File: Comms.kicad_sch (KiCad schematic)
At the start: 29 parts, among them J2 RJ45_Wuerth_7499010121A, Y1 25M

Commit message: assigned footprints
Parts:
- C1, C10, C11, C12, C13, C2, C3, C4, C5, C6, C7, C8, C9: footprint (none) -> Capacitor_SMD:C_0603_1608Metric
- D1, D2, D3, D4: footprint (none) -> LED_SMD:LED_0603_1608Metric
- R1, R2, R3, R4, R5, R6, R7, R9: footprint (none) -> Resistor_SMD:R_0603_1608Metric
- U1: footprint (none) -> Package_QFP:LQFP-64_10x10mm_P0.5mm
- Y1: footprint (none) -> Crystal:Crystal_SMD_7050-4Pin_7.0x5.0mm
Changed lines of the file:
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@@
 			)
 		)
-		(property "Footprint" ""
+		(property "Footprint" "Capacitor_SMD:C_0603_1608Metric"
 			(at 154.94 160.02 0)
 			(effects
@@
 			)
 		)
-		(property "Footprint" ""
+		(property "Footprint" "Capacitor_SMD:C_0603_1608Metric"
 			(at 109.22 171.45 0)
 			(effects
@@
 			)
 		)
-		(property "Footprint" ""
+		(property "Footprint" "LED_SMD:LED_0603_1608Metric"
 			(at 245.11 50.8 0)
 			(effects
@@
 			)
 		)
-		(property "Footprint" ""
+		(property "Footprint" "Capacitor_SMD:C_0603_1608Metric"
 			(at 243.84 99.06 0)
 			(effects
@@
 			)
 		)
-		(property "Footprint" ""
+		(property "Footprint" "Capacitor_SMD:C_0603_1608Metric"
 			(at 257.81 69.85 0)
 			(effects
@@
 			)
 		)
-		(property "Footprint" ""
+		(property "Footprint" "Capacitor_SMD:C_0603_1608Metric"
 			(at 154.94 152.4 0)
 			(effects
@@
 			)
 		)
-		(property "Footprint" ""
+		(property "Footprint" "Resistor_SMD:R_0603_1608Metric"
 			(at 259.08 30.48 0)
 			(effects
@@
 			)
 		)
-		(property "Footprint" ""
+		(property "Footprint" "Resistor_SMD:R_0603_1608Metric"
 			(at 93.98 149.86 0)
 			(effects
@@
 			)
 		)
-		(property "Footprint" ""
+		(property "Footprint" "LED_SMD:LED_0603_1608Metric"
 			(at 245.11 30.48 0)
 			(effects
@@
 			)
 		)
-		(property "Footprint" ""
+		(property "Footprint" "Package_QFP:LQFP-64_10x10mm_P0.5mm"
 			(at 74.93 60.96 0)
 			(effects
@@
 			)
 		)
-		(property "Footprint" ""
+		(property "Footprint" "Resistor_SMD:R_0603_1608Metric"
 			(at 259.08 50.8 0)
 			(effects
@@
 			)
 		)
-		(property "Footprint" ""
+		(property "Footprint" "Crystal:Crystal_SMD_7050-4Pin_7.0x5.0mm"
 			(at 246.38 76.2 0)
 			(effects
@@
 			)
 		)
-		(property "Footprint" ""
+		(property "Footprint" "Resistor_SMD:R_0603_1608Metric"
 			(at 184.15 34.29 0)
 			(effects
@@
 			)
 		)
-		(property "Footprint" ""
+		(property "Footprint" "Resistor_SMD:R_0603_1608Metric"
 			(at 95.25 160.02 0)
 			(effects
@@
 			)
 		)
-		(property "Footprint" ""
+		(property "Footprint" "Capacitor_SMD:C_0603_1608Metric"
 			(at 233.68 99.06 0)
 			(effects
@@
 			)
 		)
-		(property "Footprint" ""
+		(property "Footprint" "Resistor_SMD:R_0603_1608Metric"
 			(at 259.08 45.72 0)
 			(effects
@@
 			)
 		)
-		(property "Footprint" ""
+		(property "Footprint" "Capacitor_SMD:C_0603_1608Metric"
 			(at 223.52 99.06 0)
 			(effects
@@
 			)
 		)
-		(property "Footprint" ""
+		(property "Footprint" "Capacitor_SMD:C_0603_1608Metric"
 			(at 166.37 67.31 0)
 			(effects
@@
 			)
 		)
-		(property "Footprint" ""
+		(property "Footprint" "LED_SMD:LED_0603_1608Metric"
 			(at 245.11 25.4 0)
 			(effects
@@
 			)
 		)
-		(property "Footprint" ""
+		(property "Footprint" "Resistor_SMD:R_0603_1608Metric"
 			(at 182.88 58.42 0)
 			(effects
@@
 			)
 		)
-		(property "Footprint" ""
+		(property "Footprint" "Capacitor_SMD:C_0603_1608Metric"
 			(at 257.81 82.55 0)
 			(effects
@@
 			)
 		)
-		(property "Footprint" ""
+		(property "Footprint" "Capacitor_SMD:C_0603_1608Metric"
 			(at 265.43 99.06 0)
 			(effects
@@
 			)
 		)
-		(property "Footprint" ""
+		(property "Footprint" "Capacitor_SMD:C_0603_1608Metric"
 			(at 255.27 99.06 0)
 			(effects
@@
 			)
 		)
-		(property "Footprint" ""
+		(property "Footprint" "Capacitor_SMD:C_0603_1608Metric"
 			(at 123.19 39.37 0)
 			(effects
@@
 			)
 		)
-		(property "Footprint" ""
+		(property "Footprint" "Capacitor_SMD:C_0603_1608Metric"
 			(at 166.37 90.17 0)
 			(effects
@@
 			)
 		)
-		(property "Footprint" ""
+		(property "Footprint" "Resistor_SMD:R_0603_1608Metric"
 			(at 259.08 25.4 0)
 			(effects
@@
 			)
 		)
-		(property "Footprint" ""
+		(property "Footprint" "LED_SMD:LED_0603_1608Metric"
 			(at 245.11 45.72 0)
 			(effects

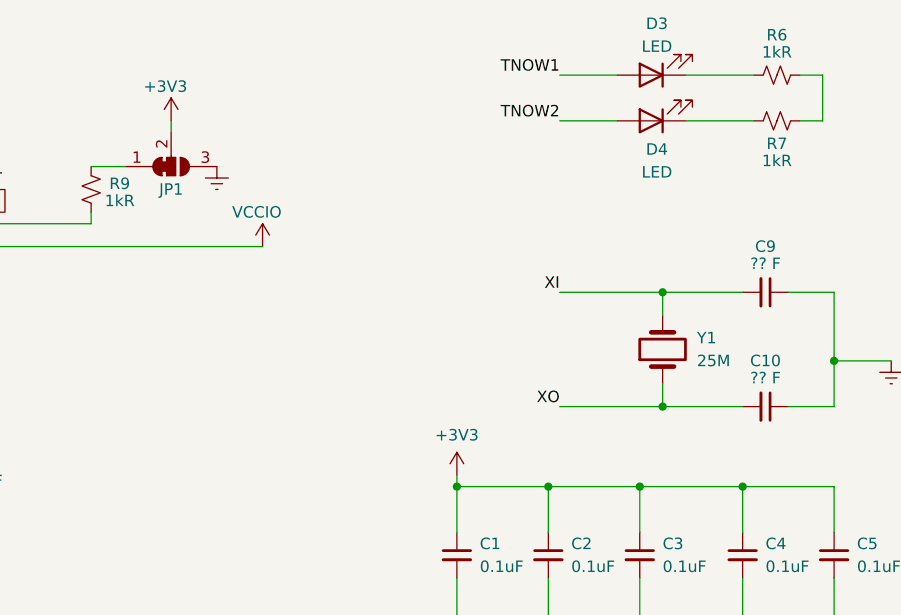
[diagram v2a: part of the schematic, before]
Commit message: routed besides mcu connections and pwoer
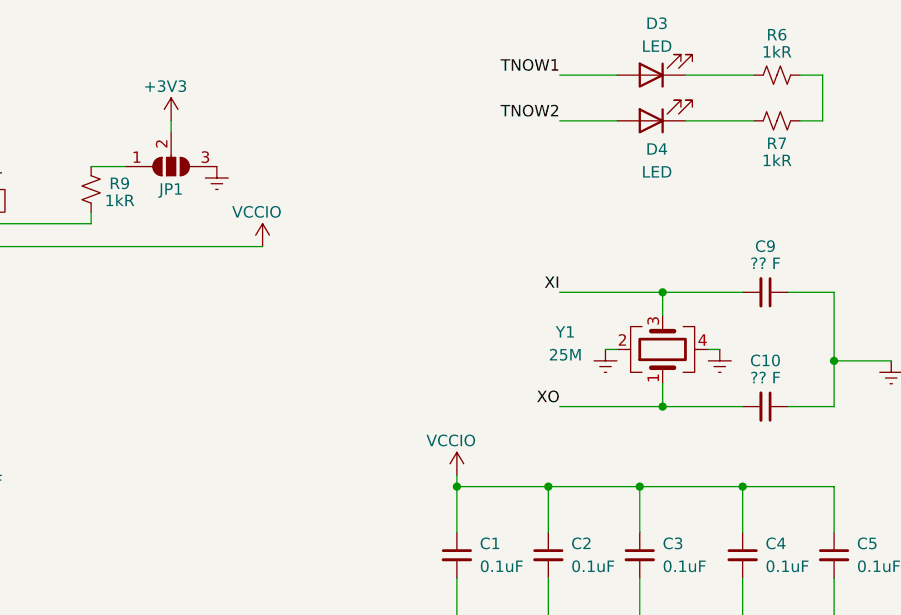
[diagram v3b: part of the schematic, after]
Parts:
- removed JP1: SolderJumper_3_Bridged12, symbol Jumper:SolderJumper_3_Bridged12
- removed Y1: 25M, Crystal:Crystal_SMD_7050-4Pin_7.0x5.0mm, symbol Device:Crystal
- added JP1: SolderJumper_3_Open, Jumper:SolderJumper-3_P1.3mm_Open_RoundedPad1.0x1.5mm_NumberLabels, symbol Jumper:SolderJumper_3_Open
- added Y1: 25M, Crystal:Crystal_SMD_7050-4Pin_7.0x5.0mm, symbol Device:Crystal_GND24
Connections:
- net +3V3: now also JP1.2 (C); no longer C1.1, C2.1, C3.1, C4.1, C5.1
- net GND: now also JP1.3 (B), Y1.2, Y1.4
- net VCCIO: now also C1.1, C2.1, C3.1, C4.1, C5.1
- net XI: now also Y1.3
- net XO: now also Y1.1
- net at R9.1: now also JP1.1 (A)

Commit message: done with my subsystem
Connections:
- net GND: now also R6.2, R7.2
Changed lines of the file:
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@@
 	)
 	(junction
+		(at 264.16 50.8)
+		(diameter 0)
+		(color 0 0 0 0)
+	)
+	(junction
 		(at 168.91 92.71)
 		(diameter 0)
@@
 	(wire
 		(pts
+			(xy 266.7 50.8) (xy 264.16 50.8)
+		)
+		(stroke
+			(width 0)
+			(type default)
+		)
+	)
+	(wire
+		(pts
 			(xy 128.27 27.94) (xy 128.27 45.72)
 		)
@@
 	(wire
 		(pts
+			(xy 266.7 52.07) (xy 266.7 50.8)
+		)
+		(stroke
+			(width 0)
+			(type default)
+		)
+	)
+	(wire
+		(pts
 			(xy 80.01 82.55) (xy 99.06 82.55)
 		)
@@
 					(unit 1)
 				)
+			)
+		)
+	)
+	(symbol
+		(lib_id "power:GNDREF")
+		(at 266.7 52.07 0)
+		(unit 1)
+		(exclude_from_sim no)
+		(in_bom yes)
+		(on_board yes)
+		(dnp no)
+		(property "Reference" "#PWR060"
+			(at 266.7 58.42 0)
+			(effects
+				(font
+					(size 1.27 1.27)
+				)
+				(hide yes)
+			)
+		)
+		(property "Value" "GND"
+			(at 266.7 56.515 0)
+			(effects
+				(font
+					(size 1.27 1.27)
+				)
+				(hide yes)
+			)
+		)
+		(property "Footprint" ""
+			(at 266.7 52.07 0)
+			(effects
+				(font
+					(size 1.27 1.27)
+				)
+				(hide yes)
+			)
+		)
+		(property "Datasheet" ""
+			(at 266.7 52.07 0)
+			(effects
+				(font
+					(size 1.27 1.27)
+				)
+				(hide yes)
+			)
+		)
+		(property "Description" "Power symbol creates a global label with name \"GNDREF\" , reference supply ground"
+			(at 266.7 52.07 0)
+			(effects
+				(font
+					(size 1.27 1.27)
+				)
+				(hide yes)
+			)
+		)
+		(pin "1"
+		)
+		(instances
+			(project "AutonomousSeedDistributor"
+				(path "/2f4a034c-8d2d-4528-8fc9-76e665033073/9dd0e49e-9fd7-43ba-89ba-9cfcf1e356cb"
+					(reference "#PWR060")
+					(unit 1)
+				)

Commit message: combined, submitted for Packaging Review
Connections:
- net GPIO_PC4 renamed B9
- net GPIO_PC5 renamed B12
- net GPIO_PC6 renamed B6
- net GPIO_PC7 renamed B7
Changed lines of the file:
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@@
 (kicad_sch
-	(version 20231120)
+	(version 20250114)
 	(generator "eeschema")
-	(generator_version "8.0")
+	(generator_version "9.0")
 	(paper "A4")
 	(title_block
@@
 	(label "TCPCS1"
 		(at 236.22 25.4 180)
-		(fields_autoplaced yes)
 		(effects
 			(font
@@
 	(label "TCPCS2"
 		(at 236.22 30.48 180)
-		(fields_autoplaced yes)
 		(effects
 			(font
@@
 	(label "TXP"
 		(at 125.73 110.49 270)
-		(fields_autoplaced yes)
 		(effects
 			(font
@@
 	(label "XI"
 		(at 234.95 69.85 180)
-		(fields_autoplaced yes)
 		(effects
 			(font
@@
 	(label "TXP"
 		(at 147.32 149.86 0)
-		(fields_autoplaced yes)
 		(effects
 			(font
@@
 	(label "ACT"
 		(at 90.17 147.32 90)
-		(fields_autoplaced yes)
 		(effects
 			(font
@@
 	(label "LINK"
 		(at 90.17 157.48 90)
-		(fields_autoplaced yes)
 		(effects
 			(font
@@
 	(label "TCPCS2"
 		(at 148.59 43.18 90)
-		(fields_autoplaced yes)
 		(effects
 			(font
@@
 	(label "XO"
 		(at 135.89 111.76 270)
-		(fields_autoplaced yes)
 		(effects
 			(font
@@
 	(label "TNOW2"
 		(at 234.95 50.8 180)
-		(fields_autoplaced yes)
 		(effects
 			(font
@@
 	(label "RXN"
 		(at 120.65 110.49 270)
-		(fields_autoplaced yes)
 		(effects
 			(font
@@
 	(label "XO"
 		(at 234.95 82.55 180)
-		(fields_autoplaced yes)
 		(effects
 			(font
@@
 	(label "TXN"
 		(at 128.27 110.49 270)
-		(fields_autoplaced yes)
 		(effects
 			(font
@@
 	(label "XI"
 		(at 133.35 111.76 270)
-		(fields_autoplaced yes)
 		(effects
 			(font
@@
 	(label "RXN"
 		(at 147.32 162.56 0)
-		(fields_autoplaced yes)
 		(effects
 			(font
@@
 	(label "TNOW1"
 		(at 90.17 62.23 180)
-		(fields_autoplaced yes)
 		(effects
 			(font
@@
 	(label "RXP"
 		(at 147.32 157.48 0)
-		(fields_autoplaced yes)
 		(effects
 			(font
@@
 	(label "LINK"
 		(at 90.17 67.31 180)
-		(fields_autoplaced yes)
 		(effects
 			(font
@@
 	(label "RXP"
 		(at 118.11 110.49 270)
-		(fields_autoplaced yes)
 		(effects
 			(font
@@
 	(label "TNOW1"
 		(at 234.95 45.72 180)
-		(fields_autoplaced yes)
 		(effects
 			(font
@@
 	(label "TNOW2"
 		(at 115.57 40.64 90)
-		(fields_autoplaced yes)
 		(effects
 			(font
@@
 	(label "TCPCS1"
 		(at 166.37 57.15 0)
-		(fields_autoplaced yes)
 		(effects
 			(font
@@
 	(label "ACT"
 		(at 90.17 64.77 180)
-		(fields_autoplaced yes)
 		(effects
 			(font
@@
 	(label "TXN"
 		(at 147.32 154.94 0)
-		(fields_autoplaced yes)
 		(effects
 			(font
@@
 		)
 	)
-	(global_label "GPIO_PC4"
+	(global_label "B9"
 		(shape input)
 		(at 140.97 38.1 90)
@@
 		)
 		(property "Intersheetrefs" "${INTERSHEET_REFS}"
-			(at 140.97 25.9224 90)
+			(at 140.97 32.6353 90)
 			(effects
 				(font
@@
 		)
 	)
-	(global_label "GPIO_PC7"
+	(global_label "B7"
 		(shape input)
 		(at 162.56 59.69 0)
@@
 		)
 		(property "Intersheetrefs" "${INTERSHEET_REFS}"
-			(at 174.7376 59.69 0)
+			(at 168.0247 59.69 0)
 			(effects
 				(font
@@
 		)
 	)
-	(global_label "GPIO_PC6"
+	(global_label "B6"
 		(shape input)
 		(at 80.01 85.09 180)
@@
 		)
 		(property "Intersheetrefs" "${INTERSHEET_REFS}"
-			(at 67.8324 85.09 0)
+			(at 74.5453 85.09 0)
 			(effects
 				(font
@@
 		)
 	)
-	(global_label "GPIO_PC5"
+	(global_label "B12"
 		(shape input)
 		(at 80.01 82.55 180)
@@
 		)
 		(property "Intersheetrefs" "${INTERSHEET_REFS}"
-			(at 67.8324 82.55 0)
+			(at 73.3358 82.55 0)
 			(effects
 				(font
